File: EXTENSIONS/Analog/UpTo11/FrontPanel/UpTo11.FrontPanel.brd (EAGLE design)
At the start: 68 x 58 mm, 6 parts

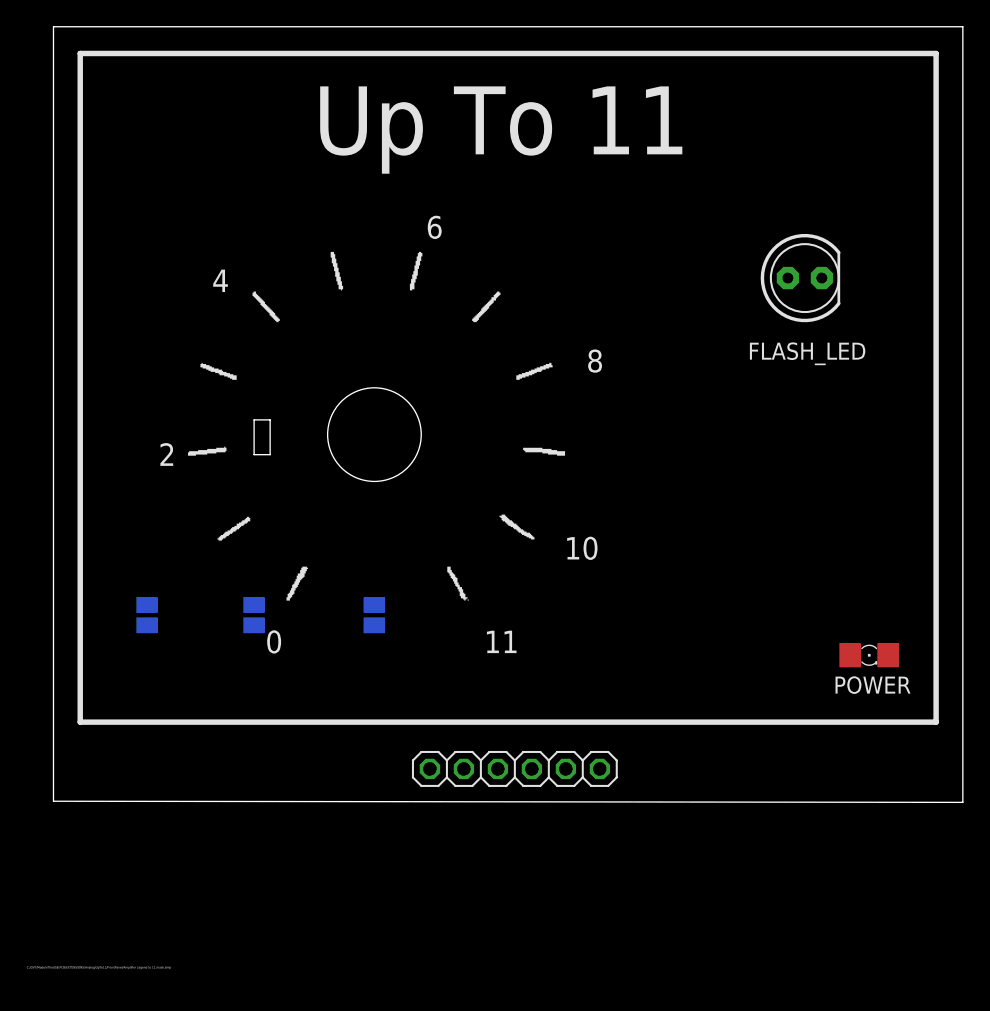
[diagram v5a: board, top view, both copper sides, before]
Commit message: Create UpTo11 Front Panel
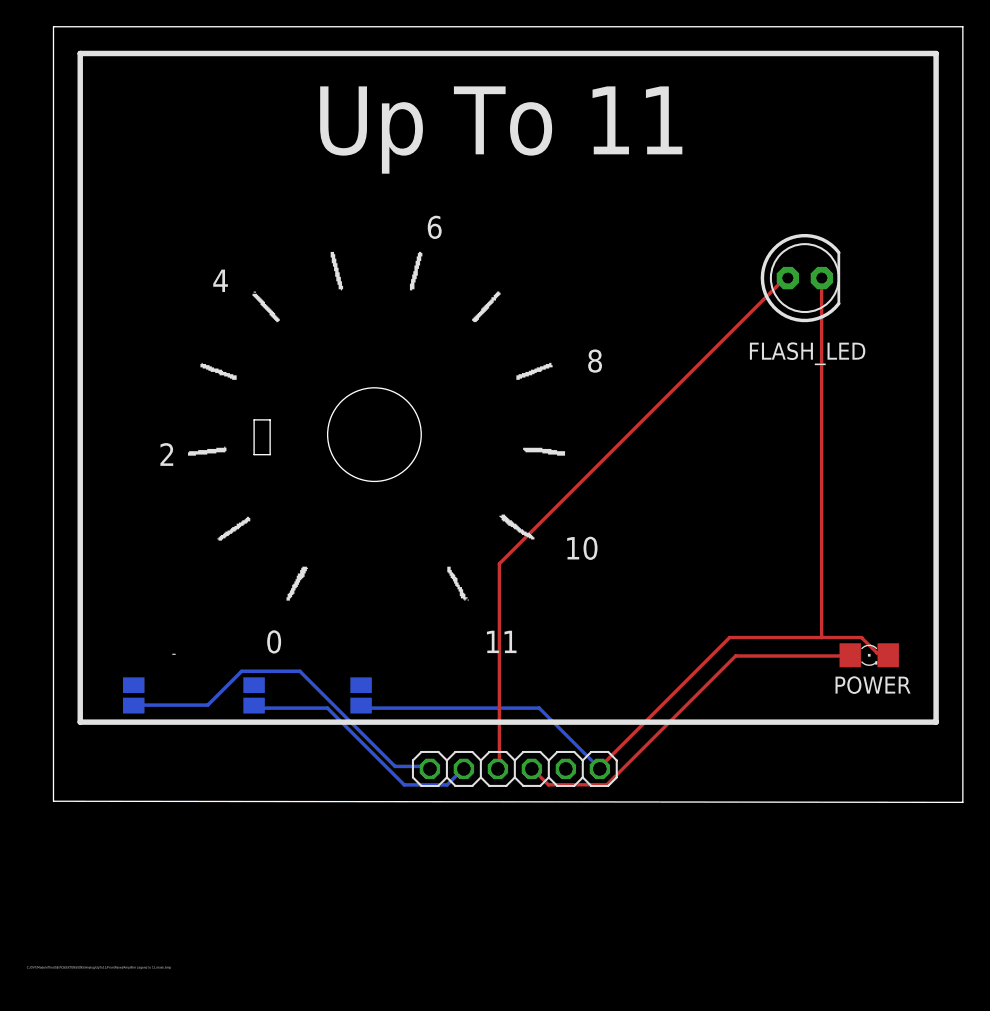
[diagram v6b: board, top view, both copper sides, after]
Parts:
- removed POT_GND_(RIGHT), POT_OUT_(LEFT): (no value), microbuilder:SOLDERJUMPER_REFLOW
- added POT_GND_(LEFT), POT_OUT_(RIGHT): (no value), microbuilder:SOLDERJUMPER_REFLOW
- moved POT_IN_(MIDDLE) 6.00 mm to (17.0, 20.0)
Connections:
- net GND_EX: now also POT_GND_(LEFT).2; no longer POT_GND_(RIGHT).2
- net POT_OUT: now also POT_OUT_(RIGHT).2; no longer POT_OUT_(LEFT).2
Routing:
- net GND_EX: track 0.00 -> 73.1 mm
- net LED_FLASH: track 0.00 -> 45.8 mm
- net LED_PWR: track 0.00 -> 28.3 mm
- net POT_OUT: track 0.00 -> 26.3 mm
- net POT_IN: track 0.00 -> 18.6 mm
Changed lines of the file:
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@@
 <layer number="23" name="tOrigins" color="15" fill="1" visible="yes" active="yes"/>
 <layer number="24" name="bOrigins" color="15" fill="1" visible="yes" active="yes"/>
-<layer number="25" name="tNames" color="7" fill="1" visible="no" active="yes"/>
-<layer number="26" name="bNames" color="7" fill="1" visible="yes" active="yes"/>
+<layer number="25" name="tNames" color="7" fill="1" visible="yes" active="yes"/>
+<layer number="26" name="bNames" color="7" fill="1" visible="no" active="yes"/>
 <layer number="27" name="tValues" color="7" fill="1" visible="yes" active="yes"/>
 <layer number="28" name="bValues" color="7" fill="1" visible="yes" active="yes"/>
@@
 <text x="66.5" y="42" size="2.1844" layer="26" rot="MR270" align="center">www.FredericTorres.com</text>
 <text x="38" y="60" size="1.6764" layer="26" rot="MR0" align="center">https://bit.ly/2Pm6jPo</text>
-<text x="43.5" y="18.5" size="1.27" layer="26" rot="MR90" align="center">GND</text>
-<text x="41" y="18" size="1.27" layer="26" rot="MR90" align="center">VCC</text>
-<text x="38.5" y="20.5" size="1.27" layer="26" rot="MR90" align="center">LED_PWR</text>
-<text x="35" y="20" size="1.27" layer="26" rot="MR90" align="center">LED_FLASH</text>
-<text x="32.5" y="20" size="1.27" layer="26" rot="MR90" align="center">POT_IN</text>
-<text x="30" y="20.5" size="1.27" layer="26" rot="MR90" align="center">POT_OUT</text>
+<text x="43.5" y="20.5" size="1.27" layer="26" rot="MR90" align="center">GND</text>
+<text x="41" y="20" size="1.27" layer="26" rot="MR90" align="center">VCC</text>
+<text x="38.5" y="21.5" size="1.27" layer="26" rot="MR90" align="center">LED_PWR</text>
+<text x="35" y="22" size="1.27" layer="26" rot="MR90" align="center">LED_FLASH</text>
+<text x="32.5" y="21" size="1.27" layer="26" rot="MR90" align="center">POT_IN</text>
+<text x="30" y="21.5" size="1.27" layer="26" rot="MR90" align="center">POT_OUT</text>
 <hole x="26" y="39.5" drill="7"/>
 <rectangle x1="17" y1="38" x2="18.2" y2="40.6" layer="46"/>
@@
 <rectangle x1="16.88518125" y1="49.94558125" x2="17.223" y2="50.03041875" layer="21"/>
 <rectangle x1="35.003" y1="49.94558125" x2="35.42718125" y2="50.03041875" layer="21"/>
-<rectangle x1="16.88518125" y1="50.03041875" x2="17.13918125" y2="50.115" layer="21"/>
+<rectangle x1="10.88518125" y1="23.03041875" x2="11.13918125" y2="23.115" layer="21"/>
 <rectangle x1="35.08681875" y1="50.03041875" x2="35.42718125" y2="50.115" layer="21"/>
 <rectangle x1="16.969" y1="50.115" x2="17.13918125" y2="50.19958125" layer="21"/>
@@
 <attribute name="VALUE" x="61.38561875" y="49.402878125" size="1.27" layer="27" ratio="10"/>
 </element>
-<element name="POT_GND_(RIGHT)" library="microbuilder" package="SOLDERJUMPER_REFLOW" value="" x="9" y="26" smashed="yes" rot="MR270">
-<attribute name="NAME" x="6.73" y="26.651" size="1.27" layer="26" ratio="18" rot="MR270" align="center"/>
-<attribute name="VALUE" x="9" y="25.5999" size="0.02" layer="28" rot="MR270"/>
+<element name="POT_GND_(LEFT)" library="microbuilder" package="SOLDERJUMPER_REFLOW" value="" x="25" y="20" smashed="yes" rot="MR270">
+<attribute name="NAME" x="22.73" y="20.651" size="1.27" layer="26" ratio="18" rot="MR270" align="center"/>
+<attribute name="VALUE" x="25" y="19.5999" size="0.02" layer="28" rot="MR270"/>
 </element>
-<element name="POT_IN_(MIDDLE)" library="microbuilder" package="SOLDERJUMPER_REFLOW" value="" x="17" y="26" smashed="yes" rot="MR270">
-<attribute name="NAME" x="14.73" y="26.651" size="1.27" layer="26" ratio="18" rot="MR270" align="center"/>
-<attribute name="VALUE" x="17" y="25.5999" size="0.02" layer="28" rot="MR270"/>
+<element name="POT_IN_(MIDDLE)" library="microbuilder" package="SOLDERJUMPER_REFLOW" value="" x="17" y="20" smashed="yes" rot="MR270">
+<attribute name="NAME" x="14.73" y="20.651" size="1.27" layer="26" ratio="18" rot="MR270" align="center"/>
+<attribute name="VALUE" x="17" y="19.5999" size="0.02" layer="28" rot="MR270"/>
 </element>
-<element name="POT_OUT_(LEFT)" library="microbuilder" package="SOLDERJUMPER_REFLOW" value="" x="26" y="26" smashed="yes" rot="MR270">
-<attribute name="NAME" x="22.73" y="26.651" size="1.27" layer="26" ratio="18" rot="MR270" align="center"/>
-<attribute name="VALUE" x="26" y="25.5999" size="0.02" layer="28" rot="MR270"/>
+<element name="POT_OUT_(RIGHT)" library="microbuilder" package="SOLDERJUMPER_REFLOW" value="" x="8" y="20" smashed="yes" rot="MR270">
+<attribute name="NAME" x="4.73" y="20.651" size="1.27" layer="26" ratio="18" rot="MR270" align="center"/>
+<attribute name="VALUE" x="8" y="19.5999" size="0.02" layer="28" rot="MR270"/>
 </element>
 </elements>
@@
 <contactref element="FRONT_PANEL_INTERFACE" pad="4"/>
 <contactref element="FLASH_LED" pad="A"/>
-<wire x1="56.91521875" y1="51.206278125" x2="35.23" y2="14.5" width="0" layer="19" extent="1-1"/>
+<wire x1="35.343" y1="29.835" x2="35.343" y2="14.688" width="0.254" layer="1"/>
+<wire x1="56.6865" y1="51.1785" x2="35.343" y2="29.835" width="0.254" layer="1"/>
+<wire x1="35.343" y1="14.688" x2="35.23" y2="14.5" width="0.254" layer="1"/>
+<wire x1="56.6865" y1="51.1785" x2="56.91521875" y2="51.206278125" width="0.254" layer="1"/>
 </signal>
 <signal name="GND_EX">
@@
 <contactref element="POWER" pad="C"/>
 <contactref element="FLASH_LED" pad="K"/>
-<contactref element="POT_GND_(RIGHT)" pad="2"/>
-<wire x1="64.422" y1="23" x2="59.45521875" y2="51.206278125" width="0" layer="19" extent="1-1"/>
-<wire x1="42.85" y1="14.5" x2="64.422" y2="23" width="0" layer="19" extent="1-1"/>
-<wire x1="9" y1="25.238" x2="42.85" y2="14.5" width="0" layer="19" extent="1-1"/>
+<contactref element="POT_GND_(LEFT)" pad="2"/>
+<wire x1="38.3265" y1="19.0485" x2="25.0155" y2="19.0485" width="0.254" layer="16"/>
+<wire x1="42.687" y1="14.688" x2="38.3265" y2="19.0485" width="0.254" layer="16"/>
+<wire x1="25.0155" y1="19.0485" x2="25" y2="19.238" width="0.254" layer="16"/>
+<wire x1="42.687" y1="14.688" x2="42.85" y2="14.5" width="0.254" layer="16"/>
+<wire x1="63.5715" y1="23.1795" x2="64.26" y2="23.1795" width="0.254" layer="1"/>
+<wire x1="62.424" y1="24.327" x2="63.5715" y2="23.1795" width="0.254" layer="1"/>
+<wire x1="52.5555" y1="24.327" x2="59.4405" y2="24.327" width="0.254" layer="1"/>
+<wire x1="59.4405" y1="24.327" x2="62.424" y2="24.327" width="0.254" layer="1"/>
+<wire x1="42.9165" y1="14.688" x2="52.5555" y2="24.327" width="0.254" layer="1"/>
+<wire x1="64.26" y1="23.1795" x2="64.422" y2="23" width="0.254" layer="1"/>
+<wire x1="42.9165" y1="14.688" x2="42.85" y2="14.5" width="0.254" layer="1"/>
+<wire x1="59.4405" y1="24.327" x2="59.4405" y2="51.1785" width="0.254" layer="1"/>
+<wire x1="59.4405" y1="51.1785" x2="59.45521875" y2="51.206278125" width="0.254" layer="1"/>
 </signal>
 <signal name="VCC">
@@
 <contactref element="FRONT_PANEL_INTERFACE" pad="3"/>
 <contactref element="POWER" pad="A"/>
-<wire x1="61.578" y1="23" x2="37.77" y2="14.5" width="0" layer="19" extent="1-1"/>
+<wire x1="53.0145" y1="22.95" x2="61.506" y2="22.95" width="0.254" layer="1"/>
+<wire x1="43.3755" y1="13.311" x2="53.0145" y2="22.95" width="0.254" layer="1"/>
+<wire x1="39.015" y1="13.311" x2="43.3755" y2="13.311" width="0.254" layer="1"/>
+<wire x1="37.8675" y1="14.4585" x2="39.015" y2="13.311" width="0.254" layer="1"/>
+<wire x1="61.506" y1="22.95" x2="61.578" y2="23" width="0.254" layer="1"/>
+<wire x1="37.8675" y1="14.4585" x2="37.77" y2="14.5" width="0.254" layer="1"/>
 </signal>
 <signal name="POT_IN">
 <contactref element="FRONT_PANEL_INTERFACE" pad="5"/>
 <contactref element="POT_IN_(MIDDLE)" pad="2"/>
-<wire x1="17" y1="25.238" x2="32.69" y2="14.5" width="0" layer="19" extent="1-1"/>
+<wire x1="22.491" y1="19.0485" x2="17.2125" y2="19.0485" width="0.254" layer="16"/>
+<wire x1="28.2285" y1="13.311" x2="22.491" y2="19.0485" width="0.254" layer="16"/>
+<wire x1="31.4415" y1="13.311" x2="28.2285" y2="13.311" width="0.254" layer="16"/>
+<wire x1="32.589" y1="14.4585" x2="31.4415" y2="13.311" width="0.254" layer="16"/>
+<wire x1="17.2125" y1="19.0485" x2="17" y2="19.238" width="0.254" layer="16"/>
+<wire x1="32.589" y1="14.4585" x2="32.69" y2="14.5" width="0.254" layer="16"/>
 </signal>
 <signal name="POT_OUT">
 <contactref element="FRONT_PANEL_INTERFACE" pad="6"/>
-<contactref element="POT_OUT_(LEFT)" pad="2"/>
-<wire x1="26" y1="25.238" x2="30.15" y2="14.5" width="0" layer="19" extent="1-1"/>
+<contactref element="POT_OUT_(RIGHT)" pad="2"/>
+<wire x1="13.5405" y1="19.278" x2="8.0325" y2="19.278" width="0.254" layer="16"/>
+<wire x1="16.065" y1="21.8025" x2="13.5405" y2="19.278" width="0.254" layer="16"/>
+<wire x1="20.4255" y1="21.8025" x2="16.065" y2="21.8025" width="0.254" layer="16"/>
+<wire x1="27.54" y1="14.688" x2="20.4255" y2="21.8025" width="0.254" layer="16"/>
+<wire x1="30.0645" y1="14.688" x2="27.54" y2="14.688" width="0.254" layer="16"/>
+<wire x1="8.0325" y1="19.278" x2="8" y2="19.238" width="0.254" layer="16"/>
+<wire x1="30.0645" y1="14.688" x2="30.15" y2="14.5" width="0.254" layer="16"/>
 </signal>
 </signals>
